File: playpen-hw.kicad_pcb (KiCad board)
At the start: 2 copper layers, 63.5 x 48.5 mm, 2 parts, among them J1 USB_C_Receptacle_USB2.0_16P, U2 STM32G473CEUx

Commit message: trying to pass DRC
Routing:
- net unconnected-(J1-SHIELD-PadS1): track 0.00 -> 18.1 mm
- net Net-(J1-GND-PadA1): track 0.00 -> 10.5 mm
- net Net-(J1-VBUS-PadA4): track 0.00 -> 6.13 mm
- net (no net): vias 8 -> 0
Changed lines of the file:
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@@
 		(layer "Edge.Cuts")
 	)
-	(via
-		(at 165.5 101.5)
-		(size 0.6)
-		(drill 0.3)
-		(layers "F.Cu" "B.Cu")
-		(net 0)
+	(segment
+		(start 123.675 95.39)
+		(end 127.605 95.39)
+		(width 0.2)
+		(layer "F.Cu")
+		(net 1)
 	)
-	(via
-		(at 163 90.5)
-		(size 0.6)
-		(drill 0.3)
-		(layers "F.Cu" "B.Cu")
-		(net 0)
+	(segment
+		(start 123.675 105.61)
+		(end 127.605 105.61)
+		(width 0.2)
+		(layer "F.Cu")
+		(net 1)
 	)
-	(via
-		(at 134.5 90.5)
-		(size 0.6)
-		(drill 0.3)
-		(layers "F.Cu" "B.Cu")
-		(net 0)
+	(segment
+		(start 123.675 105.61)
+		(end 123.675 95.39)
+		(width 0.2)
+		(layer "F.Cu")
+		(net 1)
 	)
-	(via
-		(at 148 87)
-		(size 0.6)
-		(drill 0.3)
-		(layers "F.Cu" "B.Cu")
-		(net 0)
+	(segment
+		(start 128.18 98.1)
+		(end 127.605001 98.1)
+		(width 0.2)
+		(layer "F.Cu")
+		(net 2)
 	)
-	(via
-		(at 157.5 111)
-		(size 0.6)
-		(drill 0.3)
-		(layers "F.Cu" "B.Cu")
-		(net 0)
+	(segment
+		(start 127.305 102.48241)
+		(end 127.72259 102.9)
+		(width 0.2)
+		(layer "F.Cu")
+		(net 2)
 	)
-	(via
-		(at 152.5 118)
-		(size 0.6)
-		(drill 0.3)
-		(layers "F.Cu" "B.Cu")
-		(net 0)
+	(segment
+		(start 127.72259 102.9)
+		(end 128.18 102.9)
+		(width 0.2)
+		(layer "F.Cu")
+		(net 2)
 	)
-	(via
-		(at 139 99)
-		(size 0.6)
-		(drill 0.3)
-		(layers "F.Cu" "B.Cu")
-		(net 0)
+	(segment
+		(start 127.605001 98.1)
+		(end 127.305 98.400001)
+		(width 0.2)
+		(layer "F.Cu")
+		(net 2)
 	)
-	(via
-		(at 138 110)
-		(size 0.6)
-		(drill 0.3)
-		(layers "F.Cu" "B.Cu")
-		(net 0)
+	(segment
+		(start 127.305 98.400001)
+		(end 127.305 102.48241)
+		(width 0.2)
+		(layer "F.Cu")
+		(net 2)
+	)
+	(segment
+		(start 127.815 96.935)
+		(end 126.825406 96.935)
+		(width 0.2)
+		(layer "F.Cu")
+		(net 6)
+	)
+	(segment
+		(start 128.18 97.3)
+		(end 127.815 96.935)
+		(width 0.2)
+		(layer "F.Cu")
+		(net 6)
+	)
+	(segment
+		(start 126.825406 96.935)
+		(end 126.43 97.330406)
+		(width 0.2)
+		(layer "F.Cu")
+		(net 6)
+	)
+	(segment
+		(start 126.43 97.330406)
+		(end 126.43 103.669594)
+		(width 0.2)
+		(layer "F.Cu")
+		(net 6)
+	)
+	(segment
+		(start 126.43 103.669594)
+		(end 126.825406 104.065)
+		(width 0.2)
+		(layer "F.Cu")
+		(net 6)
+	)
+	(segment
+		(start 127.815 104.065)
+		(end 128.18 103.7)
+		(width 0.2)
+		(layer "F.Cu")
+		(net 6)
+	)
+	(segment
+		(start 126.825406 104.065)
+		(end 127.815 104.065)
+		(width 0.2)
+		(layer "F.Cu")
+		(net 6)
 	)
 )

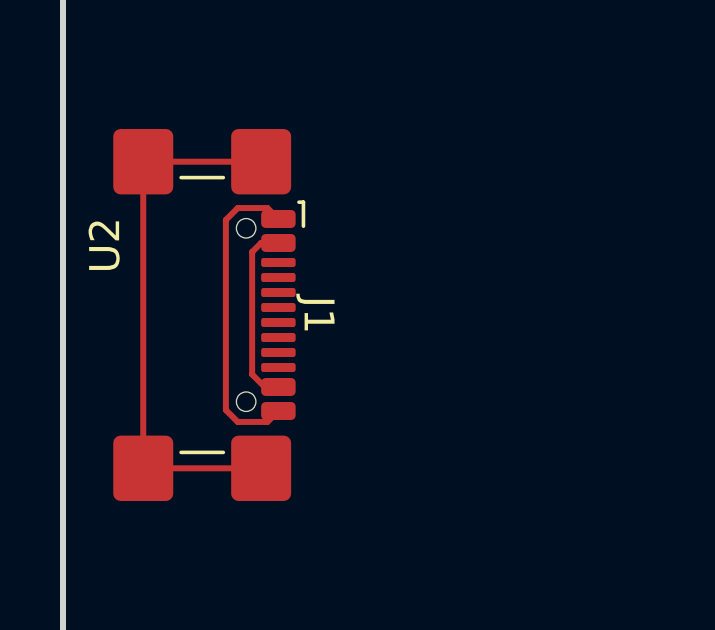
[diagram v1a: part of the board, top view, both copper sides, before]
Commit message: Trying again to pass DRC
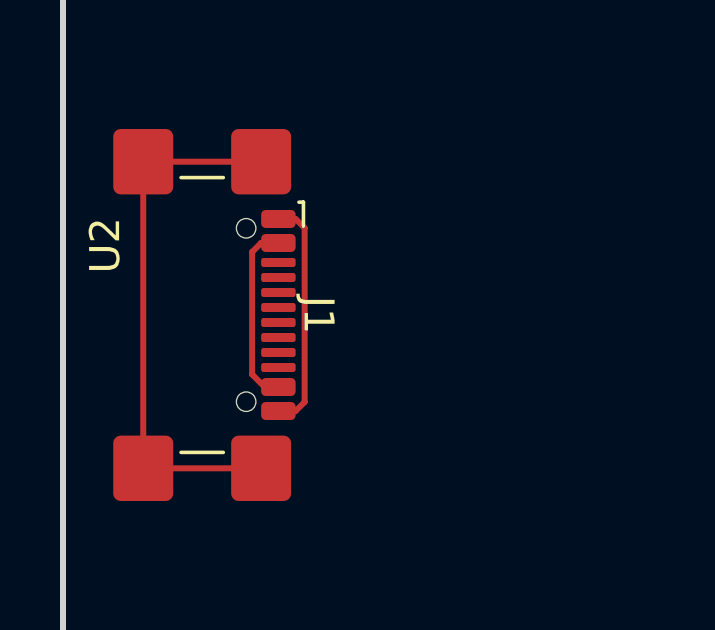
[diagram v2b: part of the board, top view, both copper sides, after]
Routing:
- net Net-(J1-GND-PadA1): track 10.5 -> 7.80 mm
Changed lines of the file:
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@@
 	)
 	(segment
-		(start 127.815 96.935)
-		(end 126.825406 96.935)
+		(start 128.754999 97.3)
+		(end 129.055 97.600001)
+		(width 0.2)
+		(layer "F.Cu")
+		(net 6)
+	)
+	(segment
+		(start 129.055 97.600001)
+		(end 129.055 103.399999)
+		(width 0.2)
+		(layer "F.Cu")
+		(net 6)
+	)
+	(segment
+		(start 129.055 103.399999)
+		(end 128.754999 103.7)
+		(width 0.2)
+		(layer "F.Cu")
+		(net 6)
+	)
+	(segment
+		(start 128.754999 103.7)
+		(end 128.18 103.7)
 		(width 0.2)
 		(layer "F.Cu")
@@
 	(segment
 		(start 128.18 97.3)
-		(end 127.815 96.935)
+		(end 128.754999 97.3)
 		(width 0.2)
 		(layer "F.Cu")
-		(net 6)
-	)
-	(segment
-		(start 126.825406 96.935)
-		(end 126.43 97.330406)
-		(width 0.2)
-		(layer "F.Cu")
-		(net 6)
-	)
-	(segment
-		(start 126.43 97.330406)
-		(end 126.43 103.669594)
-		(width 0.2)
-		(layer "F.Cu")
-		(net 6)
-	)
-	(segment
-		(start 126.43 103.669594)
-		(end 126.825406 104.065)
-		(width 0.2)
-		(layer "F.Cu")
-		(net 6)
-	)
-	(segment
-		(start 127.815 104.065)
-		(end 128.18 103.7)
-		(width 0.2)
-		(layer "F.Cu")
-		(net 6)
-	)
-	(segment
-		(start 126.825406 104.065)
-		(end 127.815 104.065)
-		(width 0.2)
-		(layer "F.Cu")
